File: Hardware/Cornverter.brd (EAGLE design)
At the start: 100 x 100 mm, 156 parts, among them IC1 LD1117S50TR, IC2 MCP4822-E_SN, IC3 TL074D, IC4 TL074D, IC5 4050D, IC6 4050D, J1 MIDI_IN (Stereo TRS), J10 Ch2 Gate Out, J11 Ch2 Trig Out, J12 Clock Out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

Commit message: added the changes from spice sims to the schematic
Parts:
- added C27, C28: 100nF, rcl:C1206
- added IC7, IC8: 4050D, 40xx:SO16
- C22, C23: value 1nF -> 33nF
- R11, R6: value 22K -> 18K
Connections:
- new net N$116: IC8.4, R38.2
- new net N$117: IC8.6, R39.2
- new net N$118: IC8.10, R40.2
- new net N$119: IC7.2, JP9.1
- new net N$120: IC7.4, JP9.2
- new net N$121: IC7.6, JP11.1
- new net N$122: IC7.10, JP11.2
- new net N$89: IC8.2, R37.2
- net +5V: now also C27.1, C28.1, IC7.1, IC8.1
- net AGND: now also C27.2, C28.2, IC7.8, IC8.8
- net CH_1_ANA_1: now also IC7.3; no longer JP9.1
- net CH_1_ANA_2: now also IC7.5; no longer JP9.2
- net CH_2_ANA_1: now also IC7.7; no longer JP11.1
- net CH_2_ANA_2: now also IC7.9; no longer JP11.2
- net N$30: now also IC8.9; no longer R40.2
- net N$34: now also IC8.7; no longer R39.2
- net N$40: now also IC8.5; no longer R38.2
- net N$44: now also IC8.3; no longer R37.2
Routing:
- net CH_1_ANA_2: track 75.5 -> 70.7 mm
- net CH_2_ANA_1: track 90.8 -> 86.0 mm
- net CH_2_ANA_2: track 72.5 -> 70.3 mm
- net N$30: track 27.7 -> 26.1 mm
- net N$44: track 19.1 -> 17.5 mm
- net N$34: track 19.1 -> 17.5 mm
- net N$40: track 26.2 -> 24.6 mm

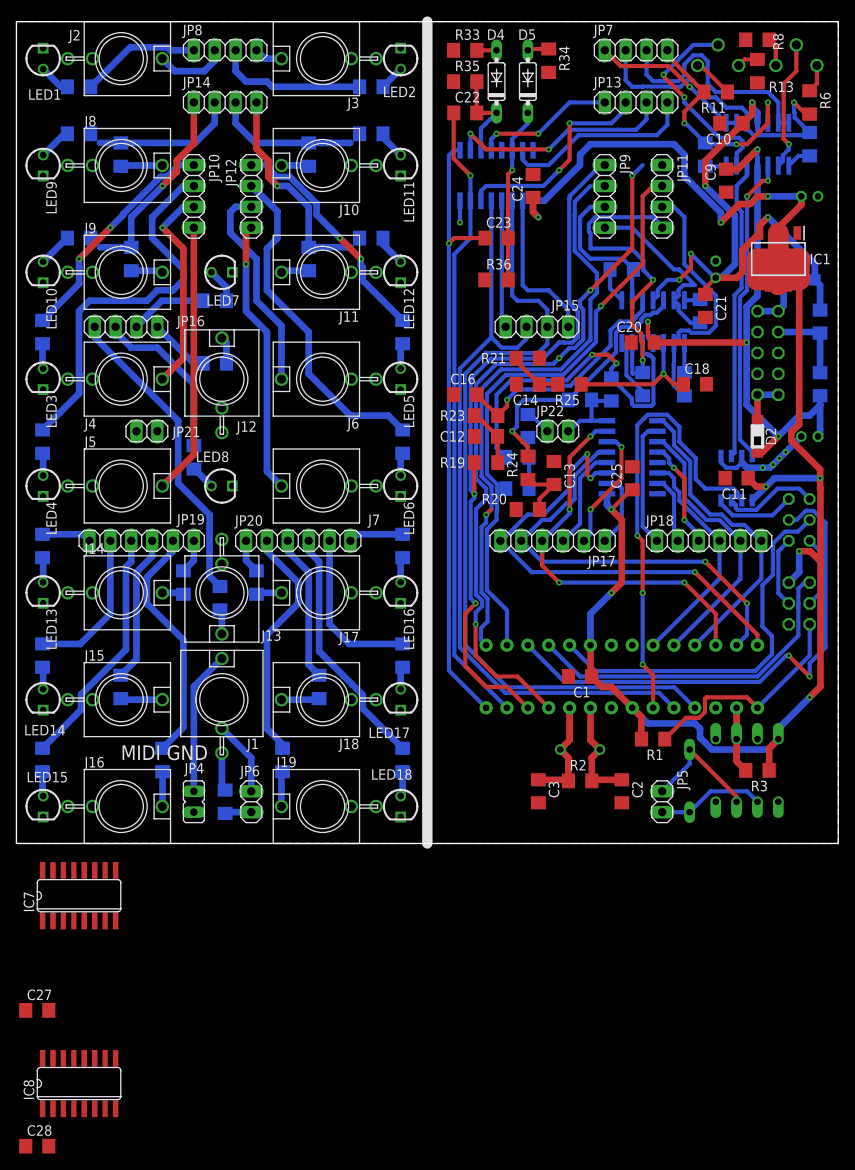
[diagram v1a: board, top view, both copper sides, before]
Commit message: updated board design for the changes to schematic and ran ERC and DRC
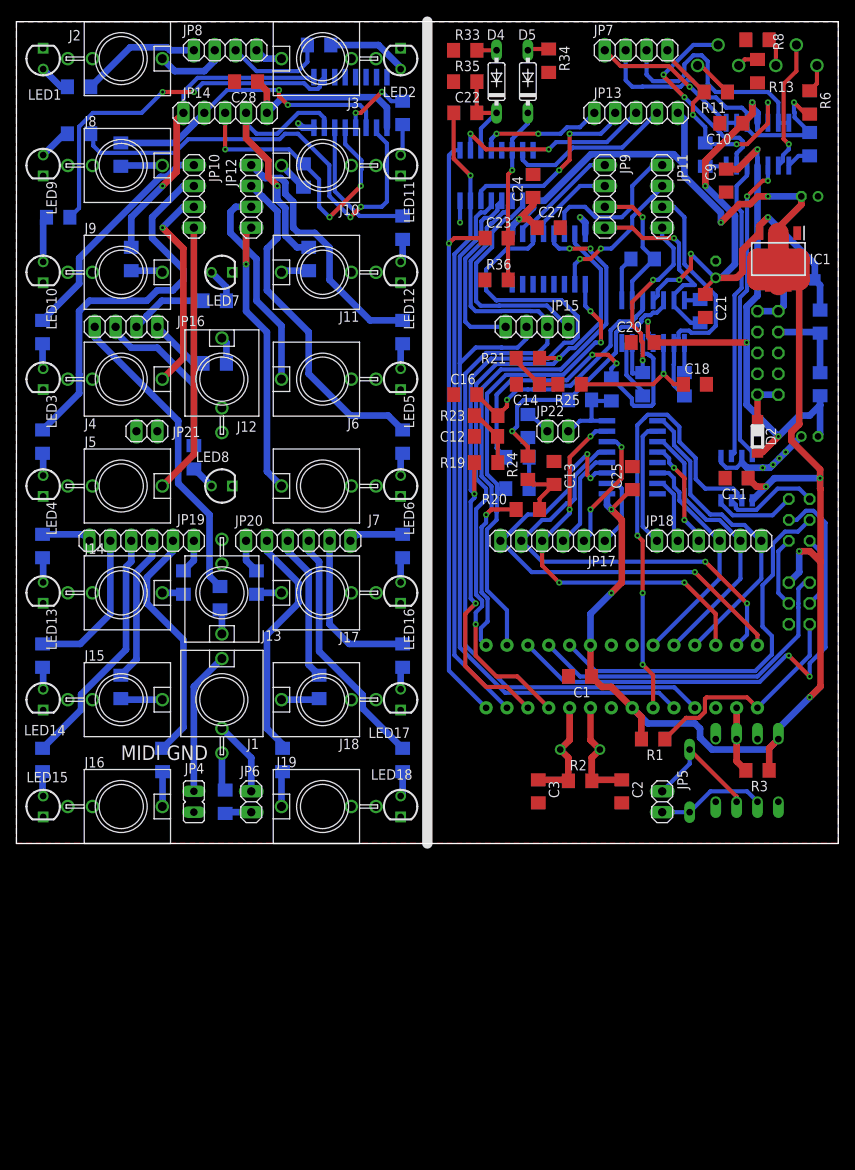
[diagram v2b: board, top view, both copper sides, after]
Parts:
- JP13: value bGate -> bGate1; device pinhead:1X04 -> pinhead:1X05
- JP14: value tGate -> tGate1; device pinhead:1X04 -> pinhead:1X05
- R11, R6: value 18K -> 100K
- R13, R8: value 100K -> 105K
- R14, R9: value 220 -> 1K
- R15, R16, R17, R18, R31, R32, R37, R38, R39, R40, R47, R48, R49, R50, R51, R52: value 220 -> 330
- moved C28 132.0 mm to (27.9, 92.7), turned to 180 degrees
- moved IC8 123.9 mm to (40.6, 90.2), flipped to the bottom
- moved C27 113.8 mm to (64.8, 74.9)
- moved IC7 96.3 mm to (64.8, 71.1), flipped to the bottom, turned to 180 degrees
- moved R14 8.13 mm to (36.8, 97.2)
- moved R39 4.58 mm to (47.0, 88.9), turned to 90 degrees
- moved R40 4.02 mm to (47.0, 74.9), turned to 90 degrees
- moved R38 3.59 mm to (5.08, 76.2)
- moved R27 2.84 mm to (76.2, 71.1)
- moved R43 2.62 mm to (34.9, 81.3)
- moved JP13 1.27 mm to (75.4, 88.9)
- moved JP14 1.27 mm to (25.4, 88.9)
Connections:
- new net TOP+5V: C28.1, IC8.1, JP14.5
- net +5V: now also JP13.5; no longer C28.1, IC8.1
- net N$116: now also IC8.10; no longer IC8.4
- net N$117: now also IC8.4; no longer IC8.6
- net N$118: now also IC8.6; no longer IC8.10
- net N$30: now also IC8.7; no longer IC8.9
- net N$34: now also IC8.5; no longer IC8.7
- net N$40: now also IC8.9; no longer IC8.5
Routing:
- net N$89: track 0.00 -> 55.4 mm, vias 0 -> 2
- net N$116: track 0.00 -> 44.8 mm, vias 0 -> 2
- net TOP+5V: track 0.00 -> 22.6 mm
- net N$121: track 0.00 -> 19.4 mm
- net N$44: track 17.5 -> 36.1 mm, vias 0 -> 2
- net N$34: track 17.5 -> 35.8 mm, vias 0 -> 3
- net N$122: track 0.00 -> 17.9 mm, vias 0 -> 2
- net N$118: track 0.00 -> 17.2 mm
- net N$73: track 40.7 -> 26.2 mm
- net N$119: track 0.00 -> 13.8 mm
- net N$40: track 24.6 -> 38.2 mm
- net CH_2_ANA_2: track 70.3 -> 58.0 mm, vias 1 -> 2
- net N$120: track 0.00 -> 10.7 mm
- net +5V: track 220.0 -> 230.5 mm
- net N$117: track 0.00 -> 9.06 mm, vias 0 -> 2
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
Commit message: Added BOM, about to check all components
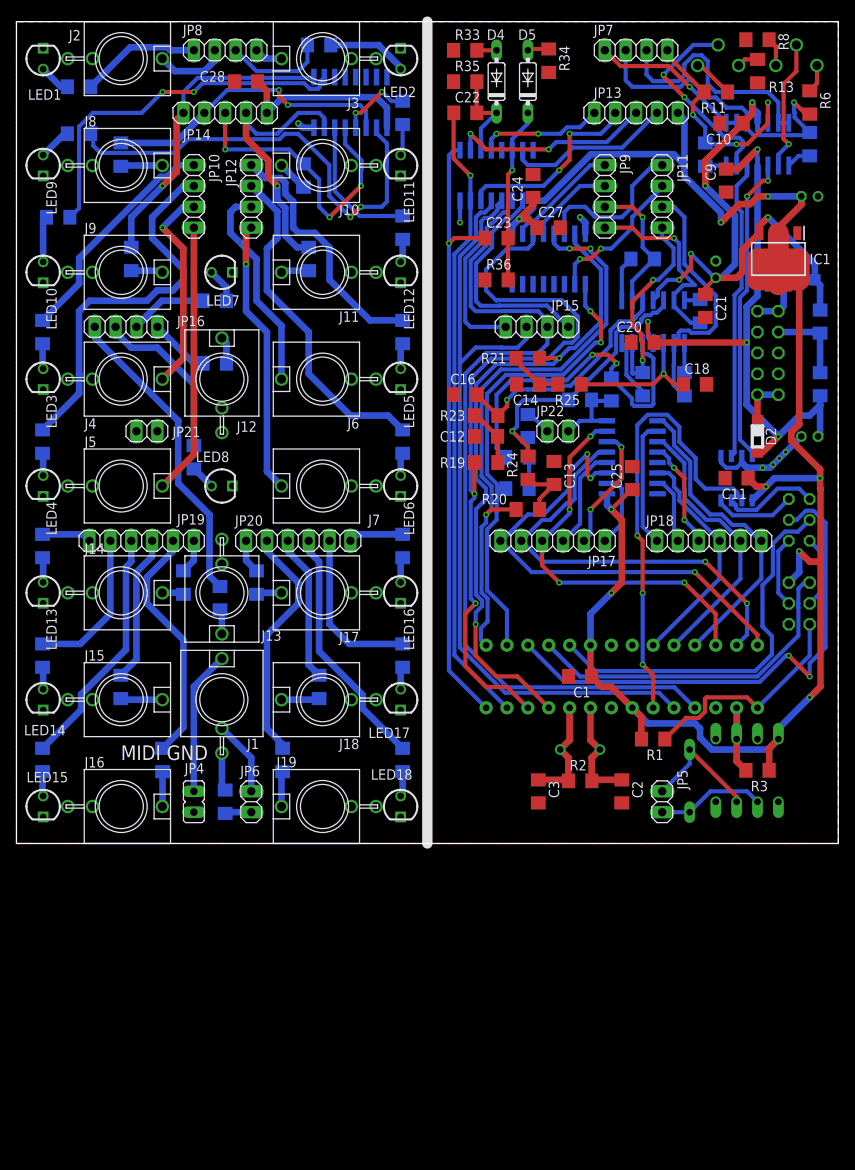
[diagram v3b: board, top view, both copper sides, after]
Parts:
- IC3, IC4: device linear:SO14 -> Improved parts:SO14

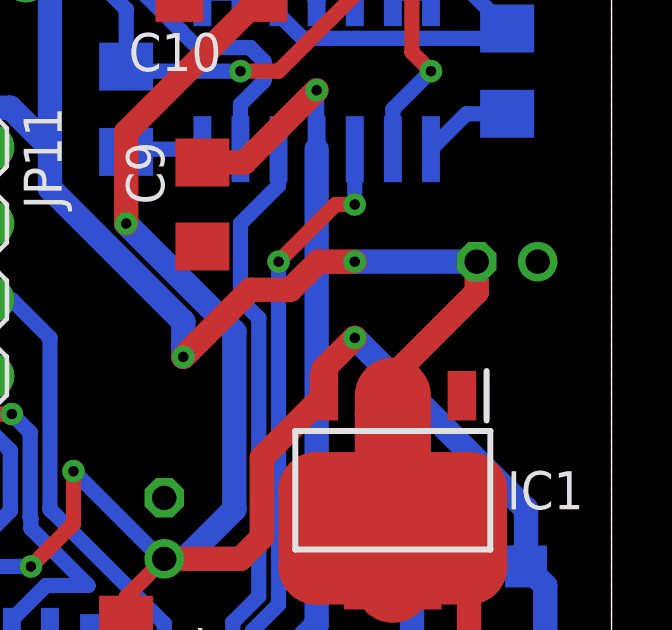
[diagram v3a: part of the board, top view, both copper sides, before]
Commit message: Changed +5V 10uF electrolytic's polarity to be correct
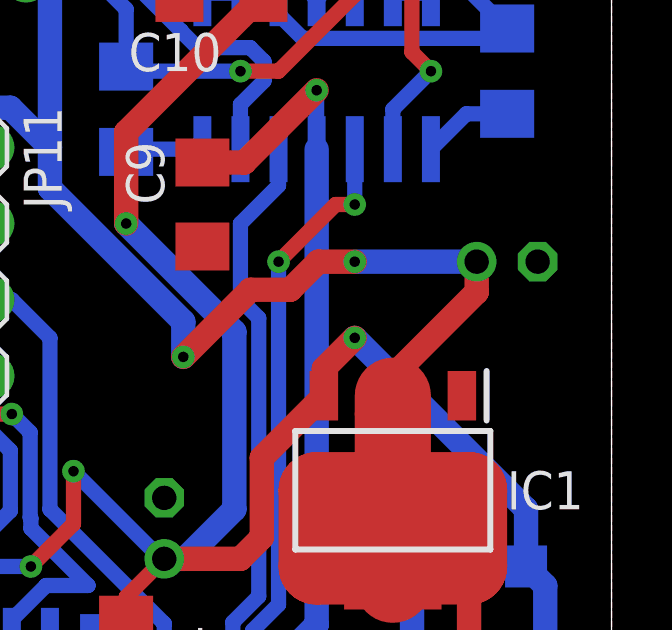
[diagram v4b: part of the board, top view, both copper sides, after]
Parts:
- turned C8 to 180 degrees
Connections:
- net +5V: now also C8.+; no longer C8.-
- net AGND: now also C8.-; no longer C8.+
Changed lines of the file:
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@@
 <attribute name="VALUE" x="100.33" y="57.15" size="1.27" layer="28" rot="MR270"/>
 </element>
-<element name="C8" library="rcl" library_urn="urn:adsk.eagle:library:334" package="E2-5" package3d_urn="urn:adsk.eagle:package:23346/2" value="10uF" x="96.52" y="78.74" smashed="yes" rot="MR0">
-<attribute name="NAME" x="94.615" y="75.946" size="1.27" layer="26" ratio="10" rot="MR0"/>
-<attribute name="SPICEPREFIX" value="C" x="96.52" y="78.74" size="1.778" layer="28" rot="MR0" display="off"/>
-<attribute name="VALUE" x="93.98" y="76.581" size="1.27" layer="28" ratio="10" rot="MR0"/>
+<element name="C8" library="rcl" library_urn="urn:adsk.eagle:library:334" package="E2-5" package3d_urn="urn:adsk.eagle:package:23346/2" value="10uF" x="96.52" y="78.74" smashed="yes" rot="MR180">
+<attribute name="NAME" x="98.425" y="81.534" size="1.27" layer="26" ratio="10" rot="MR180"/>
+<attribute name="SPICEPREFIX" value="C" x="96.52" y="78.74" size="1.778" layer="28" rot="MR180" display="off"/>
+<attribute name="VALUE" x="99.06" y="80.899" size="1.27" layer="28" ratio="10" rot="MR180"/>
 </element>
 <element name="C9" library="rcl" library_urn="urn:adsk.eagle:library:334" package="C1206" package3d_urn="urn:adsk.eagle:package:23618/2" value="100nF" x="86.36" y="80.645" smashed="yes" rot="R90">
@@
 <contactref element="U1" pad="7"/>
 <contactref element="JP1" pad="2"/>
-<contactref element="C8" pad="-"/>
 <contactref element="IC1" pad="2"/>
 <contactref element="IC1" pad="4"/>
@@
 <wire x1="95.25" y1="51.0002125" x2="95.25" y2="68.58" width="0.8128" layer="1"/>
 <wire x1="91.2025" y1="43.4175" x2="89.535" y2="41.75" width="0.8128" layer="16"/>
-<wire x1="95.504" y1="78.74" x2="95.504" y2="77.724" width="0.8128" layer="1"/>
 <wire x1="92.71" y1="74.93" x2="92.71" y2="73.66" width="0.8128" layer="1"/>
-<wire x1="95.504" y1="77.724" x2="92.71" y2="74.93" width="0.8128" layer="1"/>
+<wire x1="92.71" y1="74.93" x2="95.504" y2="77.724" width="0.8128" layer="1"/>
 <via x="91.2025" y="43.4175" extent="1-16" drill="0.35"/>
 <wire x1="89.03" y1="44.45" x2="90.0625" y2="43.4175" width="0.8128" layer="1"/>
@@
 <wire x1="85.725" y1="75.565" x2="87.963" y2="77.803" width="0.8128" layer="1"/>
 <wire x1="87.963" y1="77.803" x2="89.28811875" y2="77.803" width="0.8128" layer="1"/>
-<wire x1="91.44" y1="78.74" x2="95.504" y2="78.74" width="0.8128" layer="16"/>
 <wire x1="84.6357875" y1="11.43" x2="83.185" y2="12.8807875" width="0.8128" layer="16"/>
 <wire x1="91.44" y1="11.43" x2="84.6357875" y2="11.43" width="0.8128" layer="16"/>
@@
 <wire x1="95.25" y1="35.56" x2="96.52" y2="34.29" width="0.8128" layer="1"/>
 <wire x1="96.52" y1="34.29" x2="97.8408" y2="34.29" width="0.8128" layer="1"/>
+<contactref element="C8" pad="+"/>
+<wire x1="95.504" y1="77.724" x2="95.504" y2="78.74" width="0.8128" layer="1"/>
+<wire x1="95.504" y1="78.74" x2="91.44" y2="78.74" width="0.8128" layer="16"/>
 </signal>
 <signal name="ICSP_RST">
@@
 <contactref element="C7" pad="1"/>
 <contactref element="C6" pad="2"/>
-<contactref element="C8" pad="+"/>
 <contactref element="IC1" pad="1"/>
 <contactref element="JP4" pad="1"/>
@@
 <wire x1="34.8234" y1="87.0966" x2="34.29" y2="87.63" width="0.8128" layer="16"/>
 <via x="34.29" y="87.63" extent="1-16" drill="0.35"/>
+<contactref element="C8" pad="-"/>
 <wire x1="46.75" y1="96.77" x2="53.188" y2="96.52" width="0" layer="19" extent="1-1"/>
 </signal>

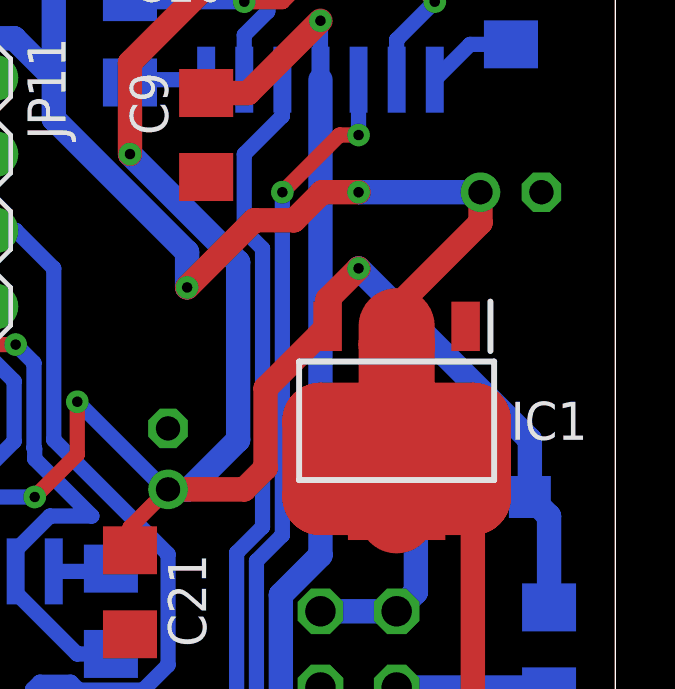
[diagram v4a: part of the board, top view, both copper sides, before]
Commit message: Added 100nF bypass cap to 5V supply
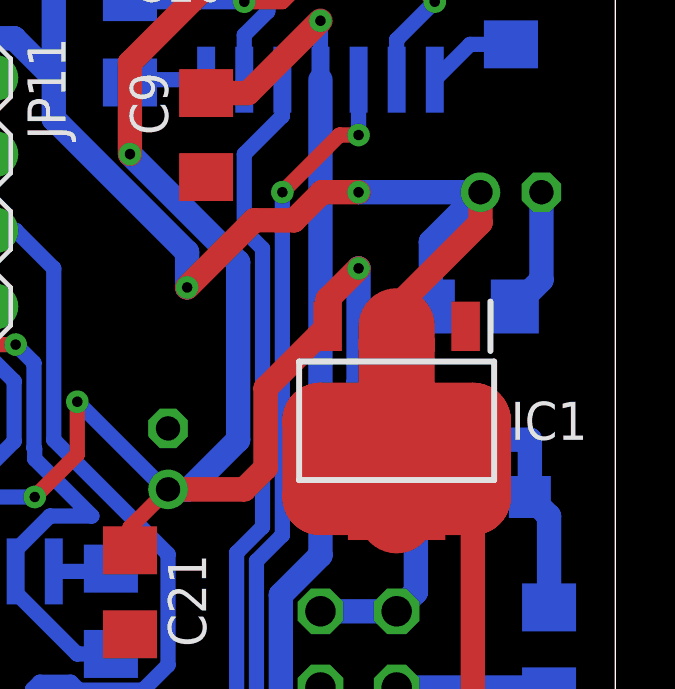
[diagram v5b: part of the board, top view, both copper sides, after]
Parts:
- added C26: 100nF, rcl:C1206
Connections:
- net +5V: now also C26.1
- net AGND: now also C26.2
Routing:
- net +5V: track 230.5 -> 235.0 mm
- net AGND: track 44.2 -> 48.4 mm
- net +12V: track 69.9 -> 72.1 mm
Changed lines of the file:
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@@
 <attribute name="VALUE" x="29.21" y="95.25" size="1.27" layer="27" rot="R180"/>
+</element>
+<element name="C26" library="rcl" library_urn="urn:adsk.eagle:library:334" package="C1206" package3d_urn="urn:adsk.eagle:package:23618/2" value="100nF" x="95.25" y="74.93" smashed="yes" rot="MR180">
+<attribute name="NAME" x="93.98" y="73.66" size="1.27" layer="26" rot="MR180"/>
+<attribute name="SPICEPREFIX" value="C" x="95.25" y="74.93" size="1.778" layer="28" rot="MR180" display="off"/>
+<attribute name="VALUE" x="93.98" y="77.47" size="1.27" layer="28" rot="MR180"/>
 </element>
 </elements>
@@
 <wire x1="95.504" y1="77.724" x2="95.504" y2="78.74" width="0.8128" layer="1"/>
 <wire x1="95.504" y1="78.74" x2="91.44" y2="78.74" width="0.8128" layer="16"/>
+<contactref element="C26" pad="1"/>
+<wire x1="93.85" y1="74.93" x2="93.85" y2="77.086" width="0.8128" layer="16"/>
+<wire x1="93.85" y1="77.086" x2="95.504" y2="78.74" width="0.8128" layer="16"/>
 </signal>
 <signal name="ICSP_RST">
@@
 <via x="34.29" y="87.63" extent="1-16" drill="0.35"/>
 <contactref element="C8" pad="-"/>
+<contactref element="C26" pad="2"/>
+<wire x1="97.536" y1="78.74" x2="97.536" y2="75.816" width="0.8128" layer="16"/>
+<wire x1="97.536" y1="75.816" x2="96.65" y2="74.93" width="0.8128" layer="16"/>
 <wire x1="46.75" y1="96.77" x2="53.188" y2="96.52" width="0" layer="19" extent="1-1"/>
 </signal>
@@
 <wire x1="90.41" y1="75.17" x2="91.44" y2="76.2" width="0.8128" layer="1"/>
 <via x="91.44" y="76.2" extent="1-16" drill="0.35"/>
-<wire x1="91.44" y1="76.2" x2="97.15" y2="70.49" width="0.8128" layer="16"/>
-<wire x1="97.15" y1="70.49" x2="97.15" y2="68.58" width="0.8128" layer="16"/>
+<wire x1="97.15" y1="68.58" x2="97.15" y2="70.49" width="0.8128" layer="16"/>
 <wire x1="97.15" y1="68.58" x2="97.79" y2="67.94" width="0.8128" layer="16"/>
 <wire x1="97.79" y1="67.94" x2="97.79" y2="64.9" width="0.8128" layer="16"/>
 <wire x1="90.17" y1="87.69" x2="90.17" y2="88.9" width="0.8128" layer="16"/>
+<wire x1="97.15" y1="70.49" x2="93.34" y2="70.49" width="0.8128" layer="16"/>
+<wire x1="91.44" y1="72.39" x2="91.44" y2="76.2" width="0.8128" layer="16"/>
+<wire x1="93.34" y1="70.49" x2="91.44" y2="72.39" width="0.8128" layer="16"/>
 </signal>
 <signal name="-12V">

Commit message: Changed value of R3 (on the MCU side of the 6n138) from 220 to 280 ohms as per midi spec
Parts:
- R3: value 220 -> 280
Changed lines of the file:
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@@
 <attribute name="VALUE" x="78.74" y="54.61" size="1.27" layer="28" rot="MR90"/>
 </element>
-<element name="R3" library="rcl" library_urn="urn:adsk.eagle:library:334" package="R1206" package3d_urn="urn:adsk.eagle:package:23540/2" value="220" x="90.17" y="8.89" smashed="yes" rot="R180">
+<element name="R3" library="rcl" library_urn="urn:adsk.eagle:library:334" package="R1206" package3d_urn="urn:adsk.eagle:package:23540/2" value="280" x="90.17" y="8.89" smashed="yes" rot="R180">
 <attribute name="NAME" x="91.44" y="7.62" size="1.27" layer="25" rot="R180"/>
 <attribute name="SPICEPREFIX" value="R" x="90.17" y="8.89" size="1.778" layer="27" rot="R180" display="off"/>
